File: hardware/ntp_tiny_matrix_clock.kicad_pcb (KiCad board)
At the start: 2 copper layers, 94 x 63 mm, 96 parts, among them J1 Barrel_Jack, J10 Conn_02x04_Odd_Even, J11 Conn_02x04_Odd_Even, J12 Conn_01x04_Male, J13 Conn_01x04_Male, J2 USB_B_Micro, J3 Conn_02x04_Odd_Even, J4 Conn_02x04_Odd_Even, J5 Conn_02x04_Odd_Even, J6 Conn_02x04_Odd_Even, J7 Conn_01x06_Male, J8 Conn_02x04_Odd_Even, J9 Conn_02x04_Odd_Even, Q1 Q_NPN_BEC, Q2 AO3401, Q3 AO3401, Q4 NJL7302L-F3, Q5 Q_NPN_BEC, Q6 Q_NPN_BEC, SW1 SW_PUSH_SMALL_H, U1 PCF8563, U2 NJW4132U2-C, U3 ESP32-WROOM, U4 W256064-XALG, U5 BME280, U6 HT16D35A, U7 JW5150A, U8 HT16D35A, U9 HT16D35A

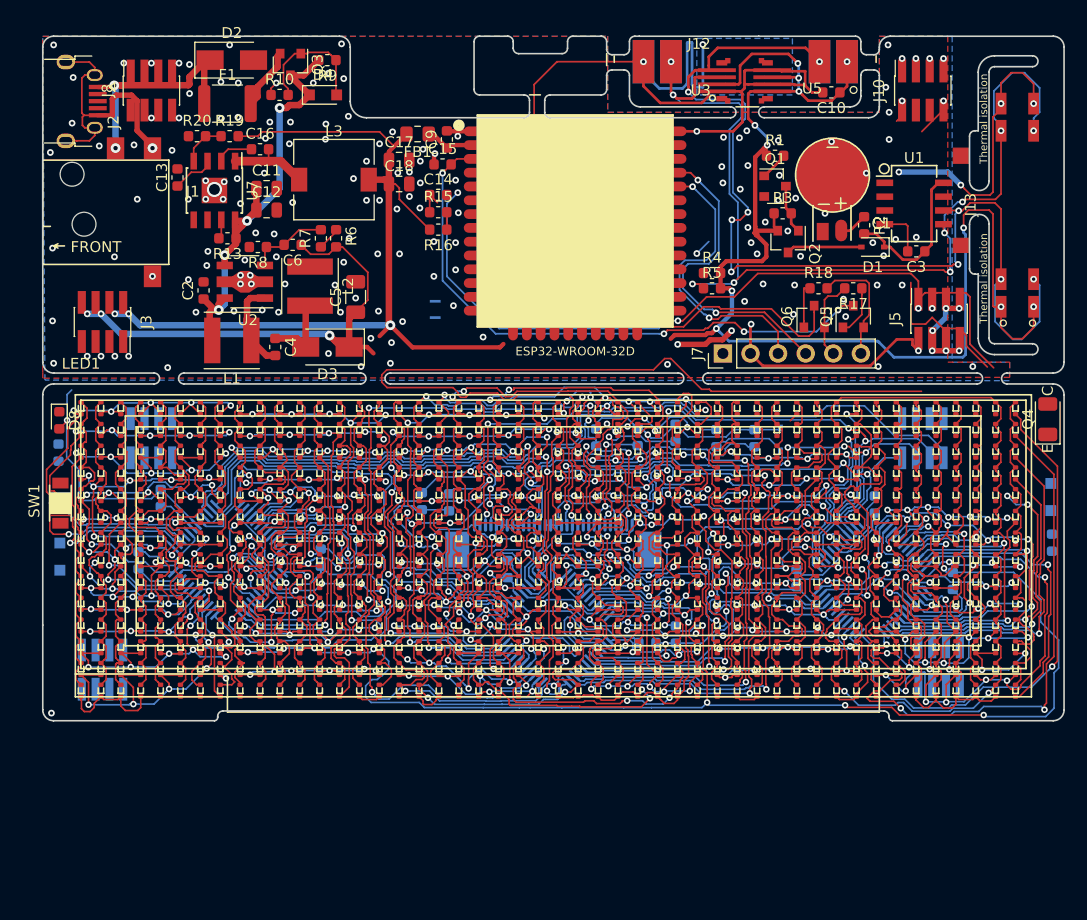
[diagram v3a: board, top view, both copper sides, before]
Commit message: Almost all connection done; Traces are too narrow to keep signal integrity but there is no space left. sigh
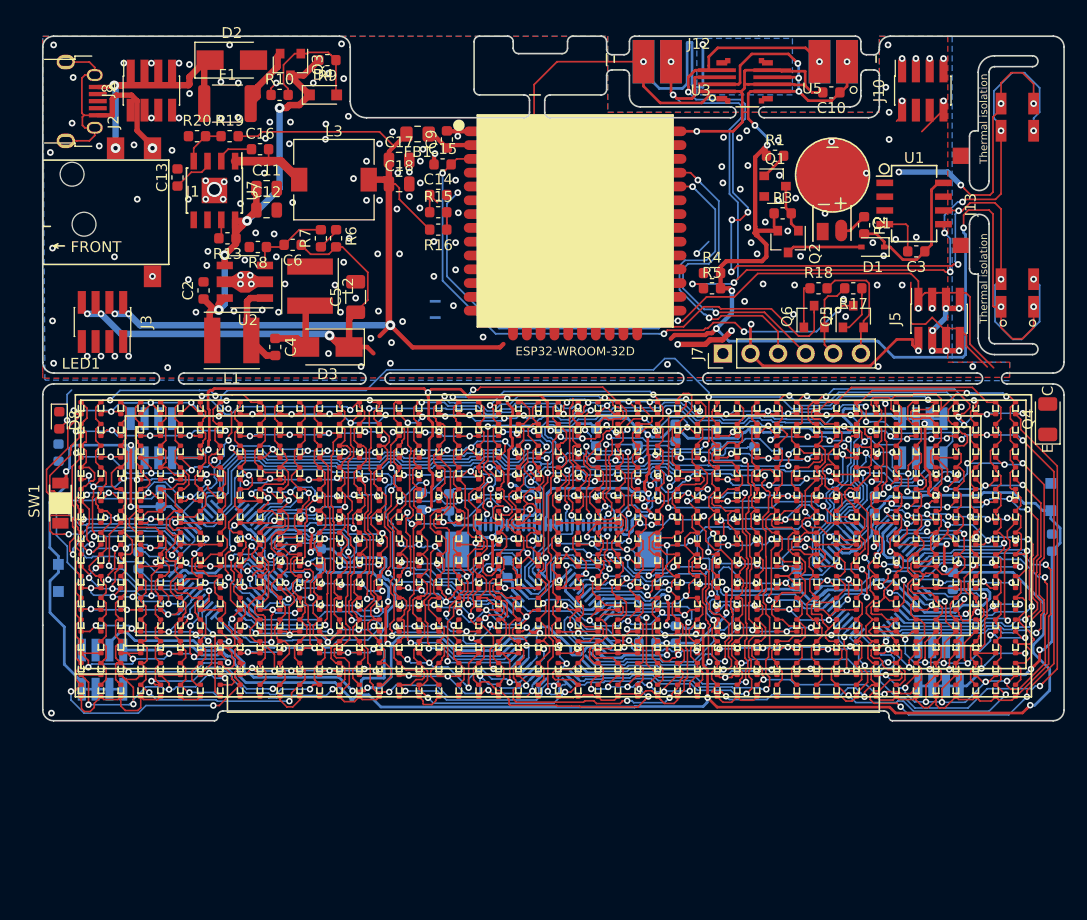
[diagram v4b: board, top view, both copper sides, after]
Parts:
- moved D6 1.96 mm to (18.4, 71.9)
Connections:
- J10 pad 2: LED_RLAT -> LED_SOUT
- J10 pad 6: LED_SOUT -> LED_RLAT
- J10 pad 7: Net-(J10-Pad7) -> GND
- J11 pad 1: LED_RLAT -> LED_SOUT
- J11 pad 5: LED_SOUT -> LED_RLAT
- J11 pad 8: Net-(J10-Pad7) -> GND
- J2 pad 2: (no net) -> Net-(J2-Pad2)
- J2 pad 3: (no net) -> Net-(J2-Pad3)
- J2 pad 4: (no net) -> Net-(J2-Pad4)
- J3 pad 1: +3V3 -> /LED_VDD
- J3 pad 3: +3V3 -> /LED_VSS
- J3 pad 7: +12V -> +3V3
- J4 pad 2: +12V -> +3V3
- J4 pad 6: +3V3 -> /LED_VSS
- J4 pad 8: +3V3 -> /LED_VDD
- J5 pad 2: Net-(J5-Pad2) -> GND
- J5 pad 4: Net-(J5-Pad2) -> GND
- J5 pad 6: Net-(J5-Pad2) -> GND
- J5 pad 8: Net-(J5-Pad2) -> GND
- J6 pad 2: Net-(J5-Pad2) -> GND
- J6 pad 4: Net-(J5-Pad2) -> GND
- J6 pad 6: Net-(J5-Pad2) -> GND
- J6 pad 8: Net-(J5-Pad2) -> GND
- J7 pad 1: (no net) -> Net-(J7-Pad1)
- U1 pad 1: (no net) -> Net-(U1-Pad1)
- U1 pad 2: (no net) -> Net-(U1-Pad2)
- U1 pad 3: (no net) -> Net-(U1-Pad3)
- U1 pad 7: (no net) -> Net-(U1-Pad7)
- U3 pad 10: (no net) -> Net-(U3-Pad10)
- U3 pad 11: (no net) -> Net-(U3-Pad11)
- U3 pad 12: (no net) -> Net-(U3-Pad12)
- U3 pad 13: (no net) -> Net-(U3-Pad13)
- U3 pad 14: (no net) -> Net-(U3-Pad14)
- U3 pad 16: (no net) -> Net-(U3-Pad16)
- U3 pad 17: (no net) -> Net-(U3-Pad17)
- U3 pad 18: (no net) -> Net-(U3-Pad18)
- U3 pad 19: (no net) -> Net-(U3-Pad19)
- U3 pad 20: (no net) -> Net-(U3-Pad20)
- U3 pad 21: (no net) -> Net-(U3-Pad21)
- U3 pad 22: (no net) -> Net-(U3-Pad22)
- U3 pad 23: (no net) -> Net-(U3-Pad23)
- U3 pad 24: (no net) -> Net-(U3-Pad24)
- U3 pad 28: (no net) -> Net-(U3-Pad28)
- U3 pad 32: (no net) -> Net-(U3-Pad32)
- U3 pad 33: (no net) -> Net-(U3-Pad33)
- U3 pad 36: (no net) -> Net-(U3-Pad36)
- U3 pad 37: (no net) -> Net-(U3-Pad37)
- U3 pad 4: (no net) -> Net-(U3-Pad4)
- U3 pad 6: (no net) -> LED_SIN
- U3 pad 9: (no net) -> Net-(U3-Pad9)
- U4 pad 11: (no net) -> Net-(U4-Pad11)
- U4 pad 20: (no net) -> Net-(U4-Pad20)
- U4 pad 21: (no net) -> Net-(U4-Pad21)
- U4 pad 23: (no net) -> Net-(U4-Pad23)
- U7 pad 5: (no net) -> Net-(U7-Pad5)
- U7 pad 6: (no net) -> Net-(U7-Pad6)
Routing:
- net GND: track 230.7 -> 433.0 mm, vias 195 -> 207
- net +3V3: track 272.1 -> 379.6 mm, vias 19 -> 25
- net LED_~SLAT: track 91.1 -> 19.7 mm
- net /LED_VSS: track 104.4 -> 139.2 mm, vias 6 -> 8
- net /k0214: track 49.0 -> 81.2 mm, vias 1 -> 5
- net /k0216: track 32.5 -> 60.3 mm, vias 1 -> 9
- net /LED_VDD: track 159.2 -> 184.0 mm, vias 10 -> 9
- net /k0217: track 28.6 -> 51.5 mm, vias 1 -> 9
- net /a0203: track 83.3 -> 102.9 mm, vias 1 -> 3
- net /a0000: track 69.7 -> 88.9 mm, vias 1 -> 3
- net /a0204: track 78.6 -> 97.7 mm, vias 1 -> 3
- net /k0201: track 14.5 -> 33.5 mm, vias 1 -> 6
- net /a0004: track 77.1 -> 95.6 mm, vias 1 -> 3
- net /a0201: track 80.1 -> 98.2 mm, vias 1 -> 3
- net /k0218: track 27.6 -> 45.5 mm, vias 3 -> 8
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
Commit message: Routing ongoing...
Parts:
- moved D6 0.91 mm to (17.8, 72.5)
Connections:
- J10 pad 1: GND -> LED_~SLAT
- J11 pad 2: GND -> LED_~SLAT
- J2 pad 2: Net-(J2-Pad2) -> (no net)
- J2 pad 3: Net-(J2-Pad3) -> (no net)
- J2 pad 4: Net-(J2-Pad4) -> (no net)
- J5 pad 1: E_AIN -> GND
- J5 pad 3: E_BUTTON -> GND
- J5 pad 5: LED_~SLAT -> GND
- J5 pad 7: STATUS -> E_AIN
- J6 pad 1: STATUS -> E_AIN
- J6 pad 3: LED_~SLAT -> GND
- J6 pad 5: E_BUTTON -> GND
- J6 pad 7: E_AIN -> GND
- J7 pad 1: Net-(J7-Pad1) -> (no net)
- J8 pad 1: /LEDVSS -> GND
- J8 pad 2: GND -> E_BUTTON
- J8 pad 3: /LEDVSS -> GND
- J8 pad 4: GND -> STATUS
- J8 pad 5: /LEDVDD -> GND
- J8 pad 7: /LEDVDD -> GND
- J9 pad 1: GND -> E_BUTTON
- J9 pad 2: /LEDVSS -> GND
- J9 pad 3: GND -> STATUS
- J9 pad 4: /LEDVSS -> GND
- J9 pad 6: /LEDVDD -> GND
- J9 pad 8: /LEDVDD -> GND
- JP1 pad 2: /LEDVDD -> (no net)
- JP2 pad 2: /LEDVSS -> (no net)
- U1 pad 1: Net-(U1-Pad1) -> (no net)
- U1 pad 2: Net-(U1-Pad2) -> (no net)
- U1 pad 3: Net-(U1-Pad3) -> (no net)
- U1 pad 7: Net-(U1-Pad7) -> (no net)
- U3 pad 10: Net-(U3-Pad10) -> (no net)
- U3 pad 11: Net-(U3-Pad11) -> (no net)
- U3 pad 12: Net-(U3-Pad12) -> (no net)
- U3 pad 13: Net-(U3-Pad13) -> (no net)
- U3 pad 14: Net-(U3-Pad14) -> (no net)
- U3 pad 16: Net-(U3-Pad16) -> (no net)
- U3 pad 17: Net-(U3-Pad17) -> (no net)
- U3 pad 18: Net-(U3-Pad18) -> (no net)
- U3 pad 19: Net-(U3-Pad19) -> (no net)
- U3 pad 20: Net-(U3-Pad20) -> (no net)
- U3 pad 21: Net-(U3-Pad21) -> (no net)
- U3 pad 22: Net-(U3-Pad22) -> (no net)
- U3 pad 23: Net-(U3-Pad23) -> (no net)
- U3 pad 24: Net-(U3-Pad24) -> (no net)
- U3 pad 28: Net-(U3-Pad28) -> (no net)
- U3 pad 32: Net-(U3-Pad32) -> (no net)
- U3 pad 33: Net-(U3-Pad33) -> (no net)
- U3 pad 36: Net-(U3-Pad36) -> (no net)
- U3 pad 37: Net-(U3-Pad37) -> (no net)
- U3 pad 4: Net-(U3-Pad4) -> (no net)
- U3 pad 6: LED_SIN -> (no net)
- U3 pad 9: Net-(U3-Pad9) -> (no net)
- U4 pad 11: Net-(U4-Pad11) -> (no net)
- U4 pad 20: Net-(U4-Pad20) -> (no net)
- U4 pad 21: Net-(U4-Pad21) -> (no net)
- U4 pad 23: Net-(U4-Pad23) -> (no net)
- U7 pad 5: Net-(U7-Pad5) -> (no net)
- U7 pad 6: Net-(U7-Pad6) -> (no net)
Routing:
- net GND: track 433.0 -> 516.9 mm, vias 207 -> 212
- net E_AIN: track 74.4 -> 2.61 mm, vias 3 -> 0
- net +12V: track 81.3 -> 143.2 mm, vias 10 -> 14
- net /LED_VDD: track 184.0 -> 220.6 mm, vias 9 -> 10
- net /LED_VSS: track 139.2 -> 166.1 mm, vias 8 -> 10
- net /k0000: track 46.1 -> 56.0 mm, vias 6 -> 9
- net /k0002: track 45.3 -> 41.1 mm, vias 6 -> 7
- net /a0001: track 90.4 -> 94.4 mm
- net /a0000: track 88.9 -> 92.2 mm
- net /a0004: track 95.6 -> 93.3 mm
- net /k0001: track 47.3 -> 45.8 mm, vias 6 -> 8
- net /a0007: track 101.8 -> 100.5 mm
- net +3V3: track 379.6 -> 380.7 mm
- net /k0215: track 73.0 -> 72.0 mm
- net /k0015: track 47.3 -> 46.4 mm
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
